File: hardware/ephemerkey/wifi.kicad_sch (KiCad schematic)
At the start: 16 parts, among them U6 AP2112K-3.3

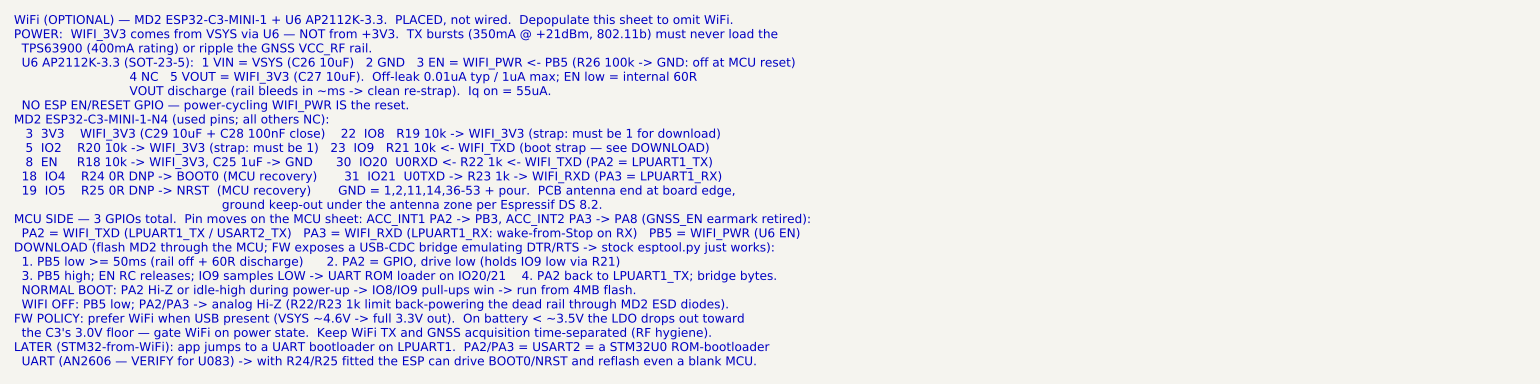
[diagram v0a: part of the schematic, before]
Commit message: hardware: gate OLED/EEPROM/I2C1 pull-ups behind PERI_EN load switch
Free the LIS3DH 2nd interrupt pin (tamper/free-fall now OR'd onto INT1 via
CTRL_REG3 I1_IA2) and repurpose it as PERI_EN. Add a high-side load switch on
the Sensors sheet (Q3 AO3401A pass FET, Q4 AO3400A gate driver, R30/R31 100k,
C31 1uF) powering a new +3V3_SW rail for DS1 OLED, U7 EEPROM, and the I2C1
pull-ups R9/R10 -- all gated off in Stop so they don't leak. LIS3DH stays on
always-on +3V3 as the wake source; FW drives PB6/PB7 low before Stop so the
powered accel never floats on the unpulled bus.

Surgical edits to both the .kicad_sch sheets and the schgen manifests (no
regen -- sheets are already partially wired). PARTS.md updated (also fills the
previously-missing Q2 AO3400A row). Also fix the lock J2 note: pin 2 = VCC <-
ephemerkey VSYS (was mislabeled "No-Connect", contradicting the wired net).

Co-Authored-By: Claude Opus 4.8 (1M context) <noreply@anthropic.com>
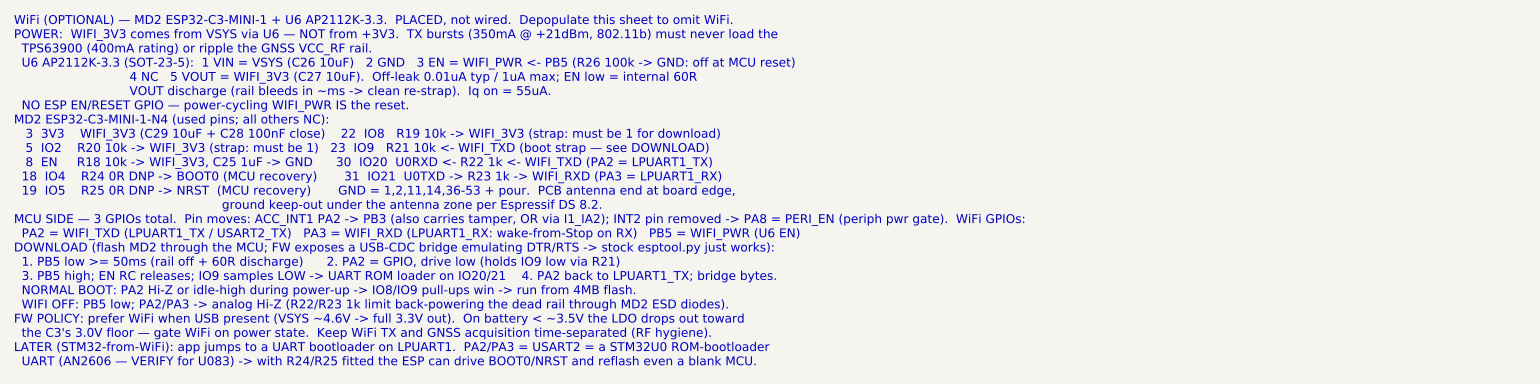
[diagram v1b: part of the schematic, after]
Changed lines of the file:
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@@
 		)
 	)
-	(text "WiFi (OPTIONAL) — MD2 ESP32-C3-MINI-1 + U6 AP2112K-3.3.  PLACED, not wired.  Depopulate this sheet to omit WiFi.\nPOWER:  WIFI_3V3 comes from VSYS via U6 — NOT from +3V3.  TX bursts (350mA @ +21dBm, 802.11b) must never load the\n  TPS63900 (400mA rating) or ripple the GNSS VCC_RF rail.\n  U6 AP2112K-3.3 (SOT-23-5):  1 VIN = VSYS (C26 10uF)   2 GND   3 EN = WIFI_PWR <- PB5 (R26 100k -> GND: off at MCU reset)\n                              4 NC   5 VOUT = WIFI_3V3 (C27 10uF).  Off-leak 0.01uA typ / 1uA max; EN low = internal 60R\n                              VOUT discharge (rail bleeds in ~ms -> clean re-strap).  Iq on = 55uA.\n  NO ESP EN/RESET GPIO — power-cycling WIFI_PWR IS the reset.\nMD2 ESP32-C3-MINI-1-N4 (used pins; all others NC):\n   3  3V3    WIFI_3V3 (C29 10uF + C28 100nF close)    22  IO8   R19 10k -> WIFI_3V3 (strap: must be 1 for download)\n   5  IO2    R20 10k -> WIFI_3V3 (strap: must be 1)   23  IO9   R21 10k <- WIFI_TXD (boot strap — see DOWNLOAD)\n   8  EN     R18 10k -> WIFI_3V3, C25 1uF -> GND      30  IO20  U0RXD <- R22 1k <- WIFI_TXD (PA2 = LPUART1_TX)\n  18  IO4    R24 0R DNP -> BOOT0 (MCU recovery)       31  IO21  U0TXD -> R23 1k -> WIFI_RXD (PA3 = LPUART1_RX)\n  19  IO5    R25 0R DNP -> NRST  (MCU recovery)       GND = 1,2,11,14,36-53 + pour.  PCB antenna end at board edge,\n                                                      ground keep-out under the antenna zone per Espressif DS 8.2.\nMCU SIDE — 3 GPIOs total.  Pin moves on the MCU sheet: ACC_INT1 PA2 -> PB3, ACC_INT2 PA3 -> PA8 (GNSS_EN earmark retired):\n  PA2 = WIFI_TXD (LPUART1_TX / USART2_TX)   PA3 = WIFI_RXD (LPUART1_RX: wake-from-Stop on RX)   PB5 = WIFI_PWR (U6 EN)\nDOWNLOAD (flash MD2 through the MCU; FW exposes a USB-CDC bridge emulating DTR/RTS -> stock esptool.py just works):\n  1. PB5 low >= 50ms (rail off + 60R discharge)      2. PA2 = GPIO, drive low (holds IO9 low via R21)\n  3. PB5 high; EN RC releases; IO9 samples LOW -> UART ROM loader on IO20/21    4. PA2 back to LPUART1_TX; bridge bytes.\n  NORMAL BOOT: PA2 Hi-Z or idle-high during power-up -> IO8/IO9 pull-ups win -> run from 4MB flash.\n  WIFI OFF: PB5 low; PA2/PA3 -> analog Hi-Z (R22/R23 1k limit back-powering the dead rail through MD2 ESD diodes).\nFW POLICY: prefer WiFi when USB present (VSYS ~4.6V -> full 3.3V out).  On battery < ~3.5V the LDO drops out toward\n  the C3's 3.0V floor — gate WiFi on power state.  Keep WiFi TX and GNSS acquisition time-separated (RF hygiene).\nLATER (STM32-from-WiFi): app jumps to a UART bootloader on LPUART1.  PA2/PA3 = USART2 = a STM32U0 ROM-bootloader\n  UART (AN2606 — VERIFY for U083) -> with R24/R25 fitted the ESP can drive BOOT0/NRST and reflash even a blank MCU."
+	(text "WiFi (OPTIONAL) — MD2 ESP32-C3-MINI-1 + U6 AP2112K-3.3.  PLACED, not wired.  Depopulate this sheet to omit WiFi.\nPOWER:  WIFI_3V3 comes from VSYS via U6 — NOT from +3V3.  TX bursts (350mA @ +21dBm, 802.11b) must never load the\n  TPS63900 (400mA rating) or ripple the GNSS VCC_RF rail.\n  U6 AP2112K-3.3 (SOT-23-5):  1 VIN = VSYS (C26 10uF)   2 GND   3 EN = WIFI_PWR <- PB5 (R26 100k -> GND: off at MCU reset)\n                              4 NC   5 VOUT = WIFI_3V3 (C27 10uF).  Off-leak 0.01uA typ / 1uA max; EN low = internal 60R\n                              VOUT discharge (rail bleeds in ~ms -> clean re-strap).  Iq on = 55uA.\n  NO ESP EN/RESET GPIO — power-cycling WIFI_PWR IS the reset.\nMD2 ESP32-C3-MINI-1-N4 (used pins; all others NC):\n   3  3V3    WIFI_3V3 (C29 10uF + C28 100nF close)    22  IO8   R19 10k -> WIFI_3V3 (strap: must be 1 for download)\n   5  IO2    R20 10k -> WIFI_3V3 (strap: must be 1)   23  IO9   R21 10k <- WIFI_TXD (boot strap — see DOWNLOAD)\n   8  EN     R18 10k -> WIFI_3V3, C25 1uF -> GND      30  IO20  U0RXD <- R22 1k <- WIFI_TXD (PA2 = LPUART1_TX)\n  18  IO4    R24 0R DNP -> BOOT0 (MCU recovery)       31  IO21  U0TXD -> R23 1k -> WIFI_RXD (PA3 = LPUART1_RX)\n  19  IO5    R25 0R DNP -> NRST  (MCU recovery)       GND = 1,2,11,14,36-53 + pour.  PCB antenna end at board edge,\n                                                      ground keep-out under the antenna zone per Espressif DS 8.2.\nMCU SIDE — 3 GPIOs total.  Pin moves: ACC_INT1 PA2 -> PB3 (also carries tamper, OR via I1_IA2); INT2 pin removed -> PA8 = PERI_EN (periph pwr gate).  WiFi GPIOs:\n  PA2 = WIFI_TXD (LPUART1_TX / USART2_TX)   PA3 = WIFI_RXD (LPUART1_RX: wake-from-Stop on RX)   PB5 = WIFI_PWR (U6 EN)\nDOWNLOAD (flash MD2 through the MCU; FW exposes a USB-CDC bridge emulating DTR/RTS -> stock esptool.py just works):\n  1. PB5 low >= 50ms (rail off + 60R discharge)      2. PA2 = GPIO, drive low (holds IO9 low via R21)\n  3. PB5 high; EN RC releases; IO9 samples LOW -> UART ROM loader on IO20/21    4. PA2 back to LPUART1_TX; bridge bytes.\n  NORMAL BOOT: PA2 Hi-Z or idle-high during power-up -> IO8/IO9 pull-ups win -> run from 4MB flash.\n  WIFI OFF: PB5 low; PA2/PA3 -> analog Hi-Z (R22/R23 1k limit back-powering the dead rail through MD2 ESD diodes).\nFW POLICY: prefer WiFi when USB present (VSYS ~4.6V -> full 3.3V out).  On battery < ~3.5V the LDO drops out toward\n  the C3's 3.0V floor — gate WiFi on power state.  Keep WiFi TX and GNSS acquisition time-separated (RF hygiene).\nLATER (STM32-from-WiFi): app jumps to a UART bootloader on LPUART1.  PA2/PA3 = USART2 = a STM32U0 ROM-bootloader\n  UART (AN2606 — VERIFY for U083) -> with R24/R25 fitted the ESP can drive BOOT0/NRST and reflash even a blank MCU."
 		(exclude_from_sim no)
 		(at 12.00 168.40 0)
